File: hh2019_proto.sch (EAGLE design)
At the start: 159 parts, among them IC1 CP210X_USB_UART, IC2 AP2114H, IC4 TP4056, J1 PJ-313D, Q1 MMBT2222A, Q3 MMBT2222A, Q4 MMBT2222A, Q5 SI1304 BDL, Q6 MMBT2222A, T1 MOSFET-PCHANNEL, T2 MOSFET-PCHANNEL, T3 MOSFET-PCHANNEL, U1 MPR121QR2, U2 ESP32-WROVER-I, U3 PCM5102A, X4 JST-PH3

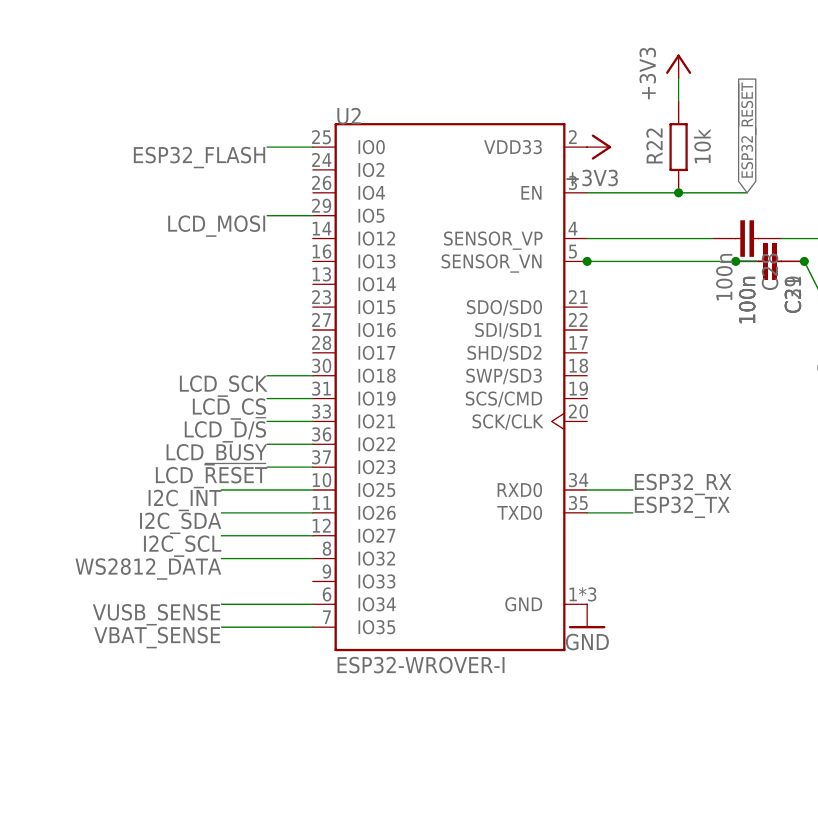
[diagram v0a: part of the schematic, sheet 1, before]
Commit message: Fixed net names on DAC
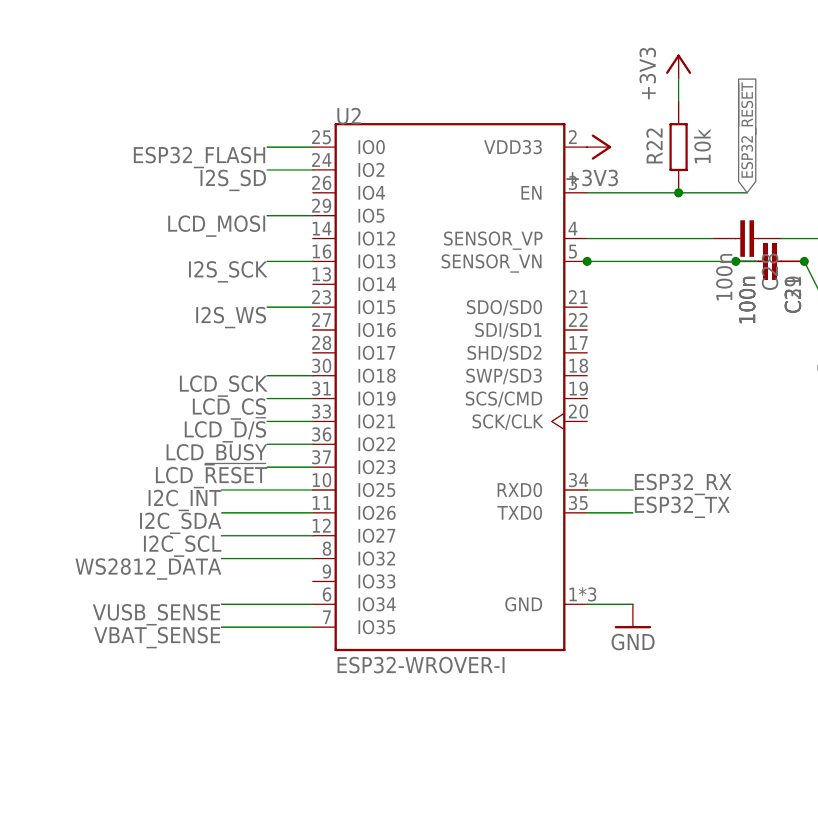
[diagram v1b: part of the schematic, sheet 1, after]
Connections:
- net I2S_SCK: now also U2.IO13
- net I2S_SD: now also U2.IO2
- net I2S_WS: now also U2.IO15
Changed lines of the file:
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@@
 <attribute name="VALUE" x="124.46" y="134.62" size="1.778" layer="96" rot="MR180"/>
 </instance>
-<instance part="GND1" gate="1" x="127" y="83.82" smashed="yes" rot="MR0">
-<attribute name="VALUE" x="129.54" y="81.28" size="1.778" layer="96" rot="MR0"/>
+<instance part="GND1" gate="1" x="132.08" y="83.82" smashed="yes" rot="MR0">
+<attribute name="VALUE" x="134.62" y="81.28" size="1.778" layer="96" rot="MR0"/>
 </instance>
 <instance part="U3" gate="G$1" x="200.66" y="73.66" smashed="yes">
@@
 <pinref part="U2" gate="G$1" pin="GND"/>
 <pinref part="GND1" gate="1" pin="GND"/>
+<wire x1="132.08" y1="86.36" x2="127" y2="86.36" width="0.1524" layer="91"/>
 </segment>
 <segment>
@@
 <wire x1="195.58" y1="127" x2="190.5" y2="127" width="0.1524" layer="91"/>
 <label x="190.5" y="127" size="1.778" layer="95" rot="R180"/>
+<label x="91.44" y="119.38" size="1.778" layer="95" rot="R180"/>
+</segment>
+<segment>
+<pinref part="U2" gate="G$1" pin="IO15"/>
+<wire x1="91.44" y1="119.38" x2="96.52" y2="119.38" width="0.1524" layer="91"/>
 </segment>
 </net>
@@
 <wire x1="195.58" y1="124.46" x2="190.5" y2="124.46" width="0.1524" layer="91"/>
 <label x="190.5" y="124.46" size="1.778" layer="95" rot="R180"/>
+<label x="91.44" y="124.46" size="1.778" layer="95" rot="R180"/>
+</segment>
+<segment>
+<pinref part="U2" gate="G$1" pin="IO13"/>
+<wire x1="91.44" y1="124.46" x2="96.52" y2="124.46" width="0.1524" layer="91"/>
 </segment>
 </net>
@@
 <wire x1="195.58" y1="121.92" x2="190.5" y2="121.92" width="0.1524" layer="91"/>
 <label x="190.5" y="121.92" size="1.778" layer="95" rot="R180"/>
-</segment>
-</net>
+<label x="91.44" y="134.62" size="1.778" layer="95" rot="R180"/>
+</segment>
+<segment>
+<pinref part="U2" gate="G$1" pin="IO2"/>
+<wire x1="91.44" y1="134.62" x2="96.52" y2="134.62" width="0.1524" layer="91"/>
+</segment>
+</net>

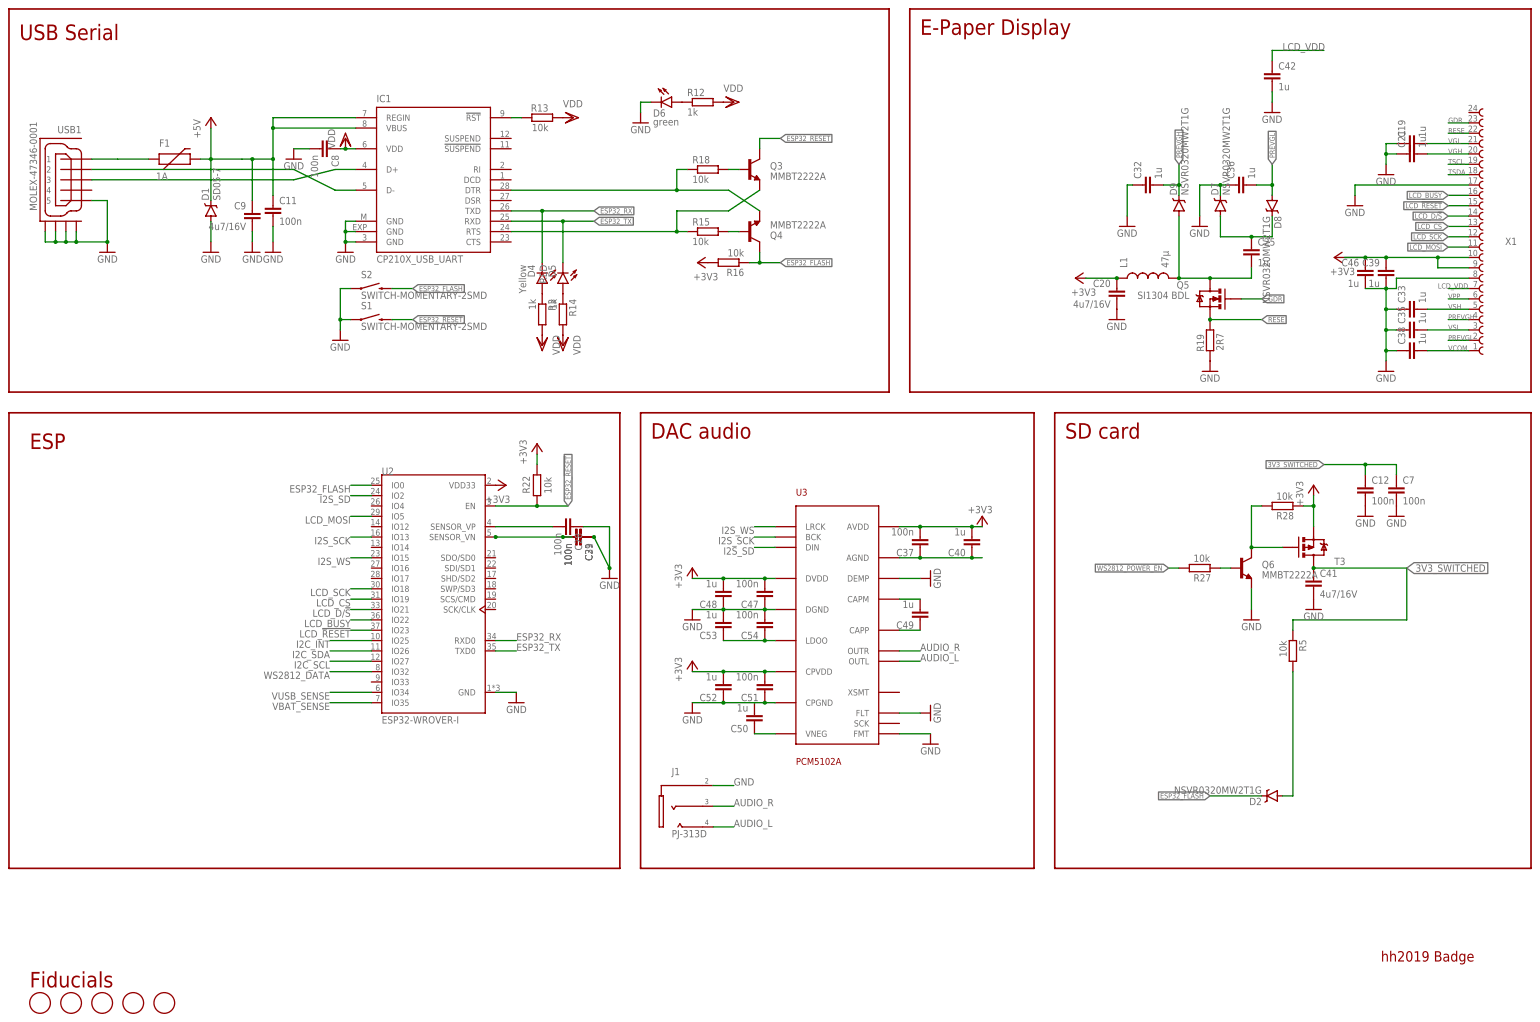
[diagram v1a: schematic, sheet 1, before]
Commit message: Fixed ESP32 net labels, removed SD card components, working on layout
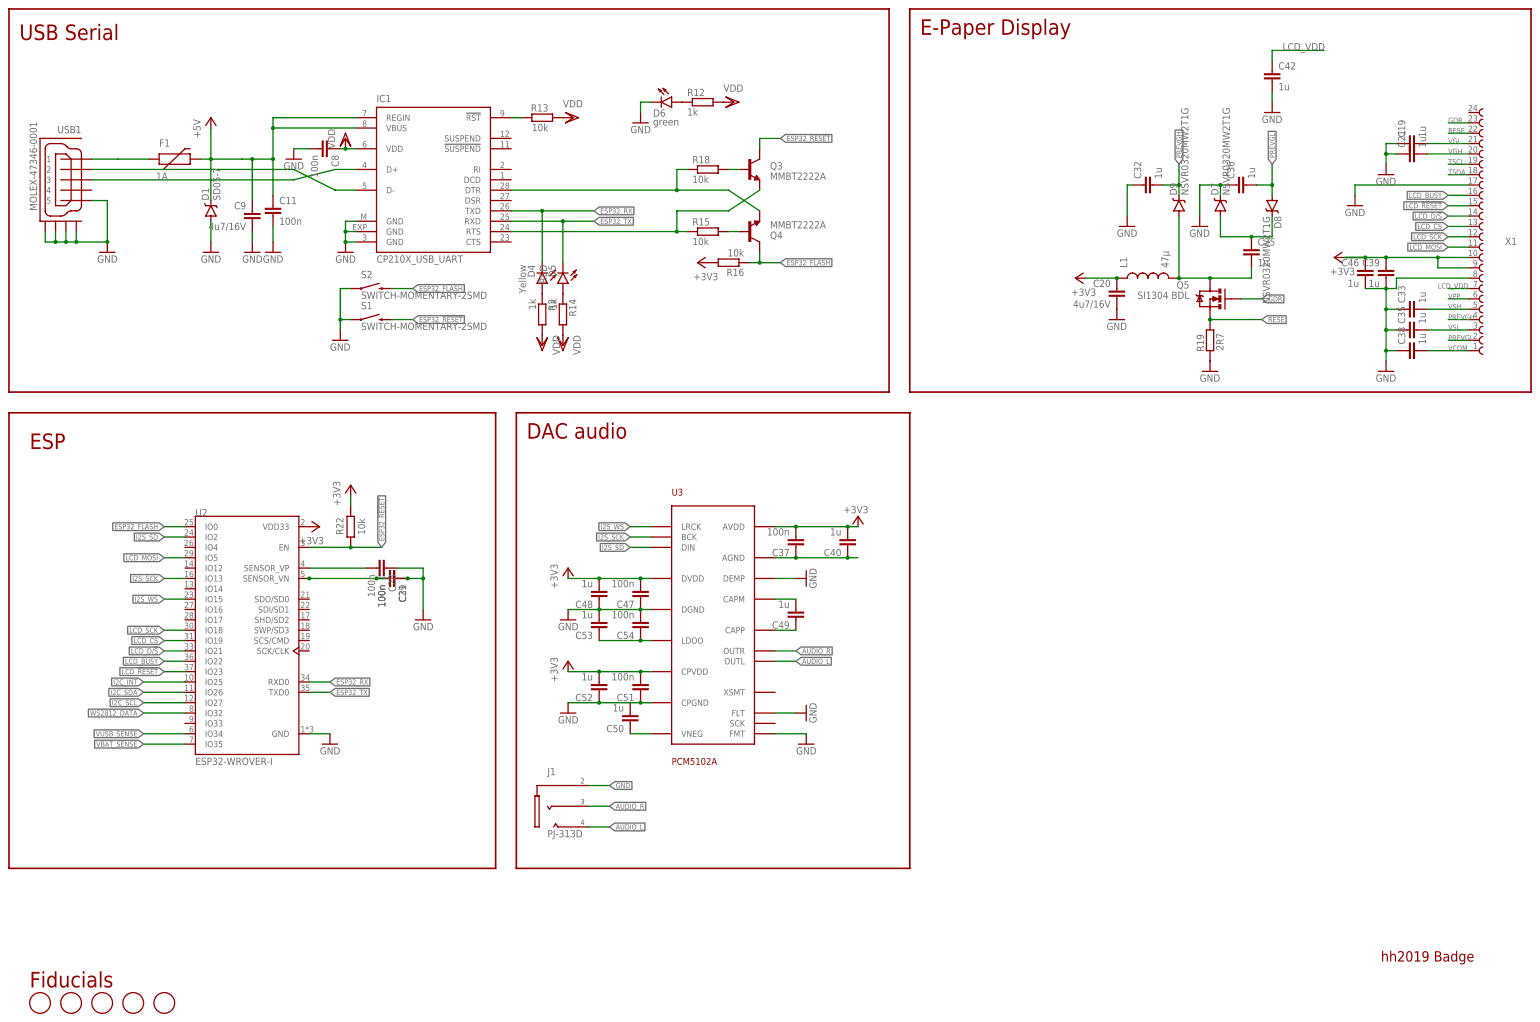
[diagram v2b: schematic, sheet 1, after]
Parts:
- removed C12, C7: 100n, hh2019_proto:C0603-DASHES
- removed C41: 4u7/16V, rcl:C-EUC0805
- removed D2: NSVR0320MW2T1G, SparkFun-DiscreteSemi:BAT20JFILM
- removed Q6: MMBT2222A, SparkFun-DiscreteSemi:TRANSISTOR_NPNMMBT2222A
- removed R27, R28, R5: 10k, 00ralf:R0603-DASHES
- removed T3: MOSFET-PCHANNEL, SparkFun-DiscreteSemi:MOSFET-PCHANNEL
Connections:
- net N$55 renamed CAPM
- net N$56 renamed CAPP
- net N$59 renamed LDO0
- net N$62 renamed VNEG
- removed net 3V3_SWITCHED: C12.1, C41.1, C7.1, R5.2, T3.D
- removed net N$15: Q6.B, R27.2
- removed net N$16: U3.OUTR
- removed net N$17: Q6.C, R28.1, T3.G
- removed net N$18: U3.OUTL
- removed net N$49: C34.1, F2.1, IC4.BAT, X43.1
- removed net SD_DATA0: D2.A, R5.1
- new net DEMP: U3.DEMP
- net 3V3: no longer R28.2, T3.S
- net AUDIO_L: now also U3.OUTL
- net AUDIO_R: now also U3.OUTR
- net ESP32_FLASH: no longer D2.C
- net GND: no longer C12.2, C41.2, C7.2, Q6.E, U3.DEMP
- net VBAT: now also C34.1, F2.1, IC4.BAT, X43.1
- net WS2812_POWER_EN: no longer R27.1
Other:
- note removed: "IO header"
- note removed: "SD card"
- moved on the sheet: C28, C29, C31, C37, C40, C47, C48, C49, C50, C51, C52, C53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

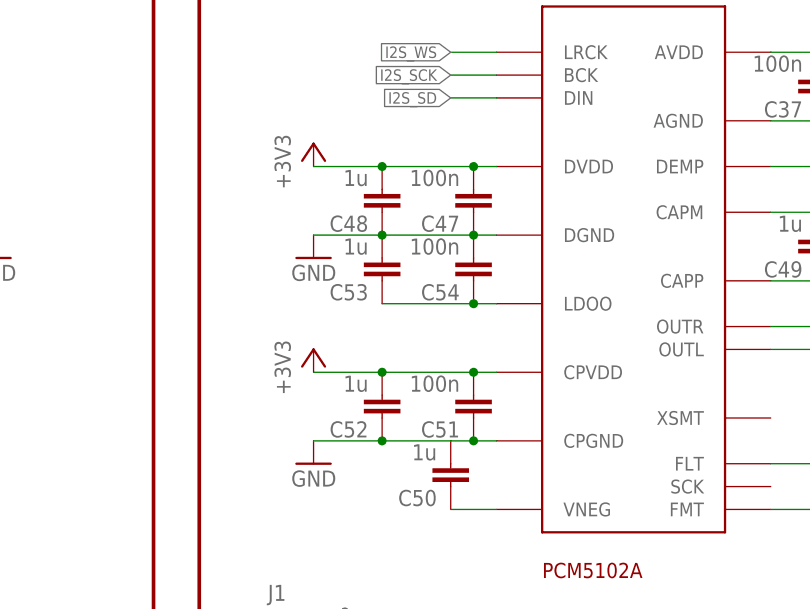
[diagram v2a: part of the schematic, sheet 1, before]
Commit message: Removed some bypass caps from DAC
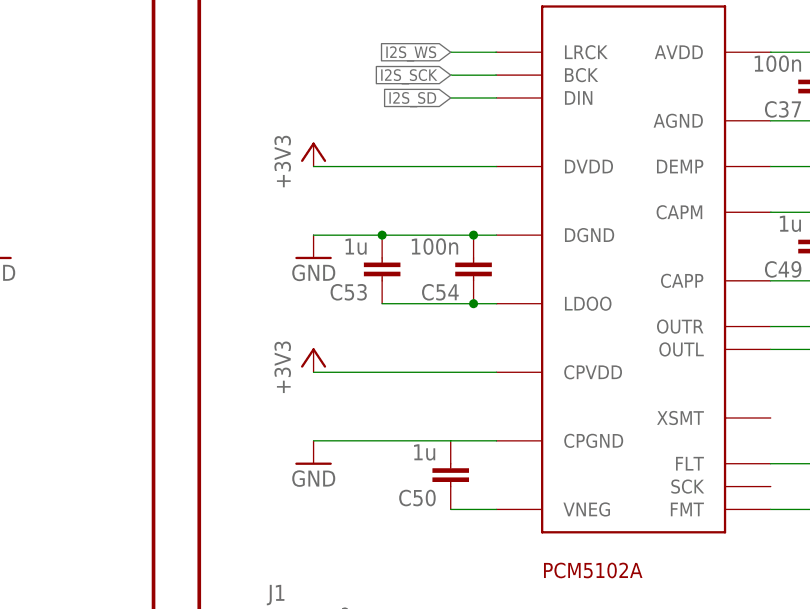
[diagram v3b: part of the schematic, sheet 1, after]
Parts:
- removed C47, C51: 100n, rcl:C-EUC0603
- removed C48, C52: 1u, rcl:C-EUC0603
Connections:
- net 3V3: no longer C47.2, C48.2, C51.2, C52.2
- net GND: no longer C47.1, C48.1, C51.1, C52.1
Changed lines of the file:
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@@
 <part name="C37" library="rcl" library_urn="urn:adsk.eagle:library:334" deviceset="C-EU" device="C0603" package3d_urn="urn:adsk.eagle:package:23616/2" value="100n"/>
 <part name="C40" library="rcl" library_urn="urn:adsk.eagle:library:334" deviceset="C-EU" device="C0603" package3d_urn="urn:adsk.eagle:package:23616/2" value="1u"/>
-<part name="C47" library="rcl" library_urn="urn:adsk.eagle:library:334" deviceset="C-EU" device="C0603" package3d_urn="urn:adsk.eagle:package:23616/2" value="100n"/>
-<part name="C48" library="rcl" library_urn="urn:adsk.eagle:library:334" deviceset="C-EU" device="C0603" package3d_urn="urn:adsk.eagle:package:23616/2" value="1u"/>
 <part name="C49" library="rcl" library_urn="urn:adsk.eagle:library:334" deviceset="C-EU" device="C0603" package3d_urn="urn:adsk.eagle:package:23616/2" value="1u"/>
 <part name="C50" library="rcl" library_urn="urn:adsk.eagle:library:334" deviceset="C-EU" device="C0603" package3d_urn="urn:adsk.eagle:package:23616/2" value="1u"/>
-<part name="C51" library="rcl" library_urn="urn:adsk.eagle:library:334" deviceset="C-EU" device="C0603" package3d_urn="urn:adsk.eagle:package:23616/2" value="100n"/>
-<part name="C52" library="rcl" library_urn="urn:adsk.eagle:library:334" deviceset="C-EU" device="C0603" package3d_urn="urn:adsk.eagle:package:23616/2" value="1u"/>
 <part name="C53" library="rcl" library_urn="urn:adsk.eagle:library:334" deviceset="C-EU" device="C0603" package3d_urn="urn:adsk.eagle:package:23616/2" value="1u"/>
 <part name="C54" library="rcl" library_urn="urn:adsk.eagle:library:334" deviceset="C-EU" device="C0603" package3d_urn="urn:adsk.eagle:package:23616/2" value="100n"/>
@@
 <attribute name="VALUE" x="211.836" y="126.619" size="1.778" layer="96" rot="R180"/>
 </instance>
-<instance part="C47" gate="G$1" x="162.56" y="109.22" smashed="yes" rot="R180">
-<attribute name="NAME" x="161.036" y="108.839" size="1.778" layer="95" rot="R180"/>
-<attribute name="VALUE" x="161.036" y="113.919" size="1.778" layer="96" rot="R180"/>
-</instance>
-<instance part="C48" gate="G$1" x="152.4" y="109.22" smashed="yes" rot="R180">
-<attribute name="NAME" x="150.876" y="108.839" size="1.778" layer="95" rot="R180"/>
-<attribute name="VALUE" x="150.876" y="113.919" size="1.778" layer="96" rot="R180"/>
-</instance>
 <instance part="C49" gate="G$1" x="200.66" y="104.14" smashed="yes" rot="R180">
 <attribute name="NAME" x="199.136" y="103.759" size="1.778" layer="95" rot="R180"/>
@@
 <attribute name="NAME" x="158.496" y="78.359" size="1.778" layer="95" rot="R180"/>
 <attribute name="VALUE" x="158.496" y="83.439" size="1.778" layer="96" rot="R180"/>
-</instance>
-<instance part="C51" gate="G$1" x="162.56" y="86.36" smashed="yes" rot="R180">
-<attribute name="NAME" x="161.036" y="85.979" size="1.778" layer="95" rot="R180"/>
-<attribute name="VALUE" x="161.036" y="91.059" size="1.778" layer="96" rot="R180"/>
-</instance>
-<instance part="C52" gate="G$1" x="152.4" y="86.36" smashed="yes" rot="R180">
-<attribute name="NAME" x="150.876" y="85.979" size="1.778" layer="95" rot="R180"/>
-<attribute name="VALUE" x="150.876" y="91.059" size="1.778" layer="96" rot="R180"/>
 </instance>
 <instance part="C53" gate="G$1" x="152.4" y="101.6" smashed="yes" rot="R180">
@@
 <segment>
 <pinref part="U3" gate="G$1" pin="CPGND"/>
-<wire x1="165.1" y1="83.82" x2="162.56" y2="83.82" width="0.1524" layer="91"/>
 <pinref part="C50" gate="G$1" pin="2"/>
-<wire x1="162.56" y1="83.82" x2="160.02" y2="83.82" width="0.1524" layer="91"/>
-<wire x1="160.02" y1="83.82" x2="152.4" y2="83.82" width="0.1524" layer="91"/>
-<pinref part="C51" gate="G$1" pin="1"/>
-<junction x="162.56" y="83.82"/>
-<pinref part="C52" gate="G$1" pin="1"/>
-<wire x1="152.4" y1="83.82" x2="144.78" y2="83.82" width="0.1524" layer="91"/>
-<junction x="152.4" y="83.82"/>
+<wire x1="165.1" y1="83.82" x2="160.02" y2="83.82" width="0.1524" layer="91"/>
+<wire x1="160.02" y1="83.82" x2="144.78" y2="83.82" width="0.1524" layer="91"/>
 <pinref part="GND18" gate="1" pin="GND"/>
 </segment>
@@
 <pinref part="U3" gate="G$1" pin="DGND"/>
 <wire x1="162.56" y1="106.68" x2="152.4" y2="106.68" width="0.1524" layer="91"/>
-<pinref part="C47" gate="G$1" pin="1"/>
 <junction x="162.56" y="106.68"/>
-<pinref part="C48" gate="G$1" pin="1"/>
 <wire x1="152.4" y1="106.68" x2="144.78" y2="106.68" width="0.1524" layer="91"/>
 <junction x="152.4" y="106.68"/>
@@
 <segment>
 <pinref part="U3" gate="G$1" pin="DVDD"/>
-<wire x1="144.78" y1="114.3" x2="152.4" y2="114.3" width="0.1524" layer="91"/>
-<pinref part="C47" gate="G$1" pin="2"/>
-<junction x="162.56" y="114.3"/>
-<pinref part="C48" gate="G$1" pin="2"/>
-<wire x1="152.4" y1="114.3" x2="162.56" y2="114.3" width="0.1524" layer="91"/>
-<junction x="152.4" y="114.3"/>
-<wire x1="162.56" y1="114.3" x2="165.1" y2="114.3" width="0.1524" layer="91"/>
+<wire x1="144.78" y1="114.3" x2="165.1" y2="114.3" width="0.1524" layer="91"/>
 <pinref part="+2V2" gate="G$1" pin="+3V3"/>
 </segment>
 <segment>
 <pinref part="U3" gate="G$1" pin="CPVDD"/>
-<wire x1="165.1" y1="91.44" x2="162.56" y2="91.44" width="0.1524" layer="91"/>
-<pinref part="C51" gate="G$1" pin="2"/>
-<wire x1="162.56" y1="91.44" x2="152.4" y2="91.44" width="0.1524" layer="91"/>
-<junction x="162.56" y="91.44"/>
-<pinref part="C52" gate="G$1" pin="2"/>
-<wire x1="152.4" y1="91.44" x2="144.78" y2="91.44" width="0.1524" layer="91"/>
-<junction x="152.4" y="91.44"/>
+<wire x1="165.1" y1="91.44" x2="144.78" y2="91.44" width="0.1524" layer="91"/>
 <pinref part="+2V3" gate="G$1" pin="+3V3"/>
 </segment>

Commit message: Prepping layout
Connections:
- net N$12 renamed CE
- net N$7 renamed PROG
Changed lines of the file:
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@@
 </instance>
 <instance part="D5" gate="G$1" x="143.51" y="186.69" smashed="yes" rot="R180">
-<attribute name="NAME" x="139.954" y="191.262" size="1.778" layer="95" rot="R270"/>
-<attribute name="VALUE" x="137.795" y="191.262" size="1.778" layer="96" rot="R270"/>
+<attribute name="NAME" x="150.114" y="191.262" size="1.778" layer="95" rot="R270"/>
+<attribute name="VALUE" x="147.955" y="191.262" size="1.778" layer="96" rot="R270"/>
 </instance>
 <instance part="D6" gate="G$1" x="170.18" y="231.14" smashed="yes" rot="R270">
@@
 </segment>
 </net>
-<net name="N$7" class="0">
+<net name="PROG" class="0">
 <segment>
 <pinref part="IC4" gate="G$1" pin="PROG"/>
@@
 <pinref part="R32" gate="G$1" pin="1"/>
 <wire x1="160.02" y1="144.78" x2="170.18" y2="144.78" width="0.1524" layer="91"/>
-<wire x1="170.18" y1="144.78" x2="186.69" y2="144.78" width="0.1524" layer="91"/>
+<wire x1="170.18" y1="144.78" x2="177.8" y2="144.78" width="0.1524" layer="91"/>
 <junction x="170.18" y="144.78"/>
-<label x="180.34" y="144.78" size="1.778" layer="95"/>
+<label x="180.34" y="144.78" size="1.778" layer="95" xref="yes"/>
+<wire x1="177.8" y1="144.78" x2="179.07" y2="144.78" width="0.1524" layer="91"/>
+<wire x1="180.34" y1="144.78" x2="179.07" y2="144.78" width="0.1524" layer="91"/>
 </segment>
 <segment>
@@
 </segment>
 </net>
-<net name="N$12" class="2">
+<net name="CE" class="2">
 <segment>
 <pinref part="IC4" gate="G$1" pin="VCC"/>
